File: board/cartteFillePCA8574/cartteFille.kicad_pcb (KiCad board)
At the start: 2 copper layers, 60 x 100 mm, 69 parts, among them U1 LM358, U201 PCA8574D,518, U202 PCA8574D,518, U21-2 SN74LVC2G14DBVTG4, U23-4 SN74LVC2G14DBVTG4, U25-6 SN74LVC2G14DBVTG4, U27-8 SN74LVC2G14DBVTG4

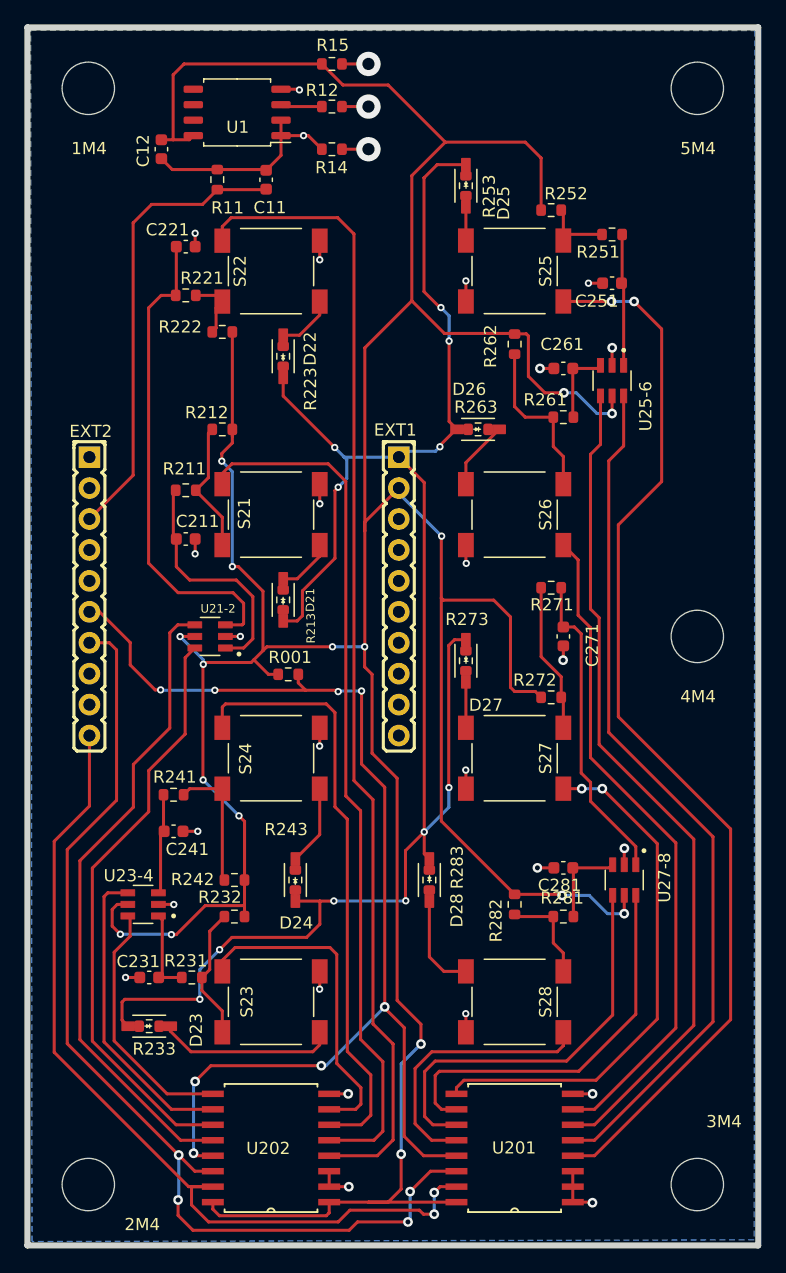
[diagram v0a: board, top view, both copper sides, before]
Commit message: Review_GPIO_Replaced
version avant la review du pcb avec les nouveau gpio
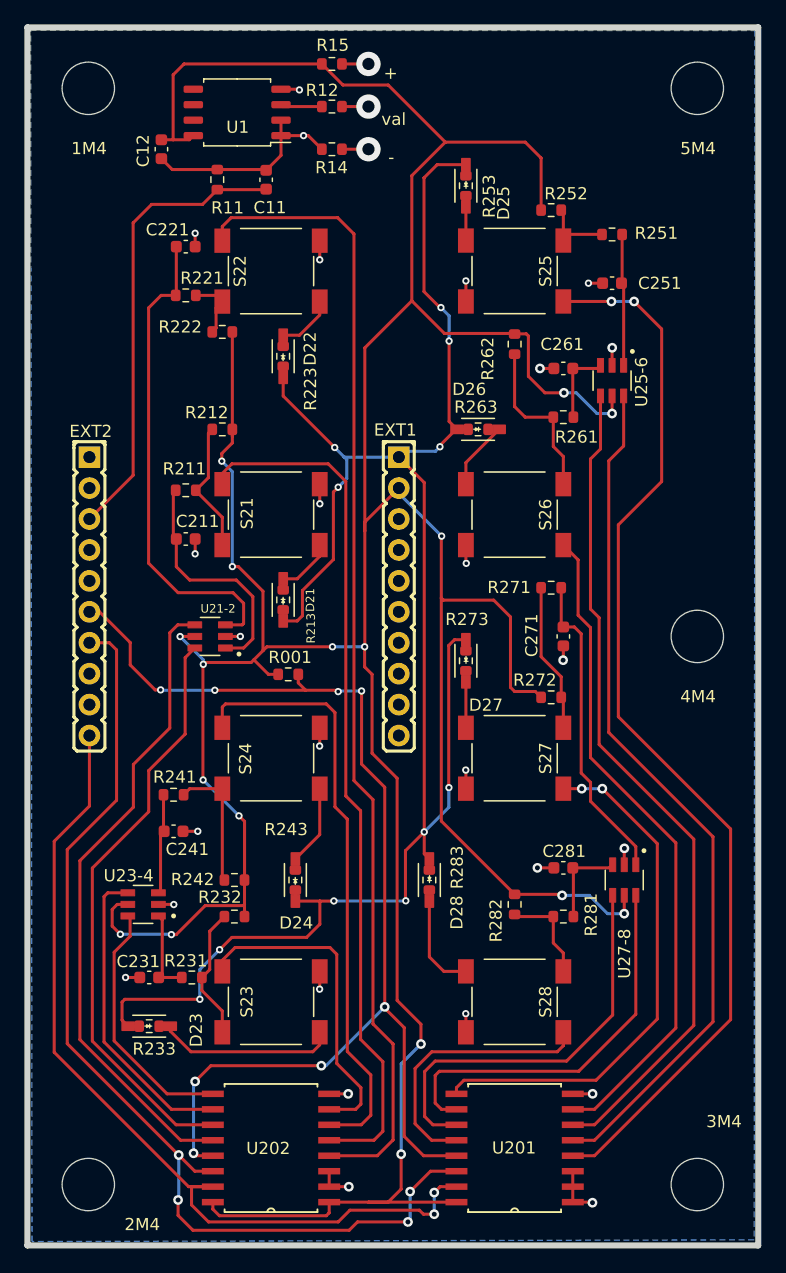
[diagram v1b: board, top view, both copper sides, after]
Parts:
- R001: value 10kOhm -> 10k
- R11, R231: value 10KOhm -> 10K
- R272: value 1KOhm -> 1K
- U21-2, U23-4: value SN74LVC2G14DBVTG4 -> SN74
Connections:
- net /U20GPA0-S26LED renamed /U201P3-S26LED
- net /U20GPA1-S25LED renamed /U201P0-S25LED
- net /U20GPA2-S28LED renamed /U201P7-S28LED
- net /U20GPA3-S27LED renamed /U201P4-S27LED
- net /U20GPA4-S22LED renamed /U202P0-S22LED
- net /U20GPA5-S21LED renamed /U202P1-S21LED
- net /U20GPA6-S24LED renamed /U202P2-S24LED
- net /U20GPA7-S23LED renamed /U202P3-S23LED
- net /U20GPB0-U234S23 renamed /U202P4-U234S23
- net /U20GPB1-U234S24 renamed /U202P5-U234S24
- net /U20GPB2-U212S21 renamed /U202P6-U212S21
- net /U20GPB3-U212S22 renamed /U202P7-U212S22
- net /U20GPB4-U278S27 renamed /U201P5-U278S27
- net /U20GPB5-U278S28 renamed /U201P6-U278S28
- net /U20GPB6-U256S25 renamed /U201P1-U256S25
- net /U20GPB7-U256S26 renamed /U201P2-U256S26
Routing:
- net +5V: track 157.1 -> 157.9 mm
- net /GPIO32-INTB: track 97.0 -> 96.4 mm
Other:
- board text added: "+"
- board text added: "-"
- board text added: "val"
